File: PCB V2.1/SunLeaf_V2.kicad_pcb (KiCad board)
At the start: 4 copper layers, 77 x 40 mm, 111 parts, among them IC1 ESP_09, J1 20021121-00010C4LF, J10 B4B-PH-K-S(LF)(SN), J11 B4B-PH-K-S(LF)(SN), J12 B4B-PH-K-S(LF)(SN), J13 B4B-PH-K-S(LF)(SN), J14 B4B-PH-K-S(LF)(SN), J15 B4B-PH-K-S(LF)(SN), J16 B4B-PH-K-S(LF)(SN), J2 0475890001-MicroUSBPort, J3 B2B-PH-K-S(LF)(SN), J4 B3B-PH-K-S(LF)(SN), J5 B4B-PH-K-S(LF)(SN), J6 B4B-PH-K-S(LF)(SN), J7 B4B-PH-K-S(LF)(SN), J8 B4B-PH-K-S(LF)(SN), J9 B4B-PH-K-S(LF)(SN), P1 CONN_01X04, Q1 DMG2307L-7, Q2 DMG2307L-7, SW1 B3U-1000P, SW2 B3U-1000P, T1 1909763-1, U1 STM32F446RET6_-_TQFP64, U2 BQ24210DQCT, U3 AZ1117CR-3.3TRG1_1, U4 74HC4052D, U5 PCA9518DBQR, X1 ABM3B8.000MHZB2T, X2 ABS07-32.768KHZ-9-T

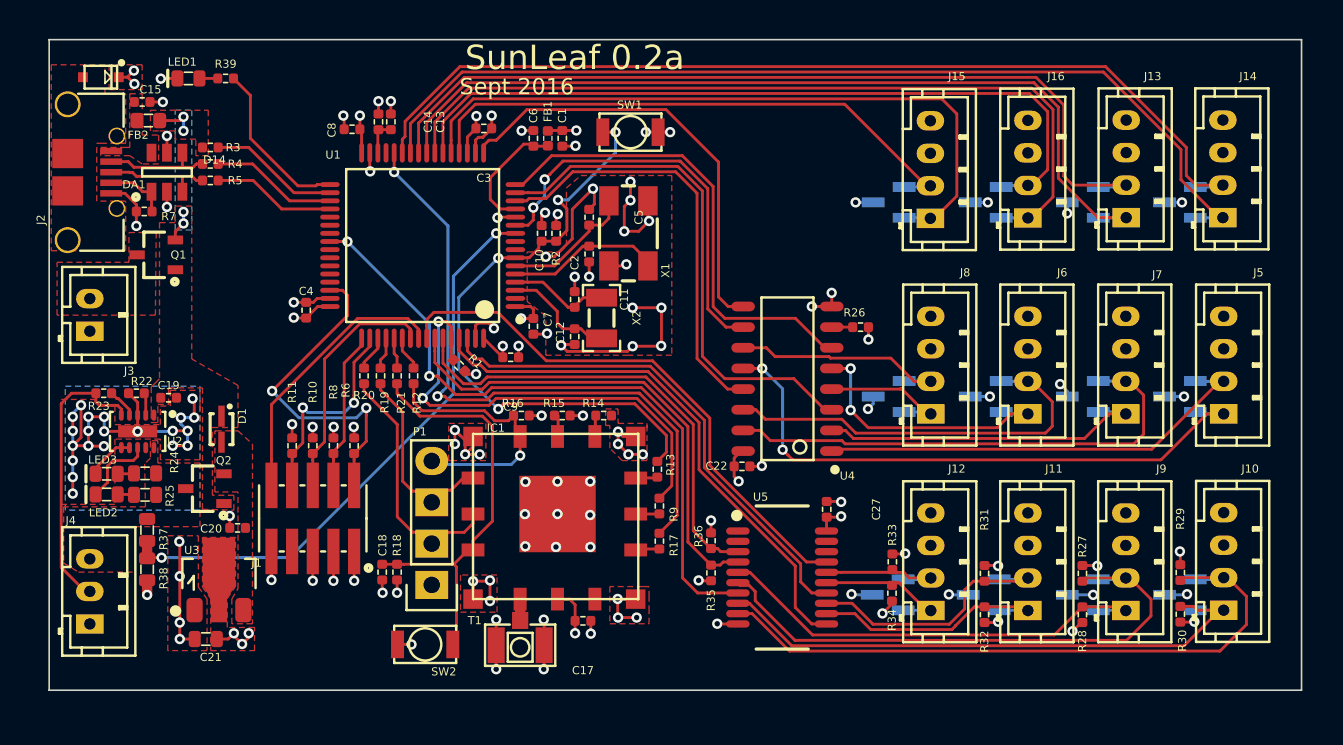
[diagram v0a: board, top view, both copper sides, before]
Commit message: App Notes
App notes added to datasheets folder.
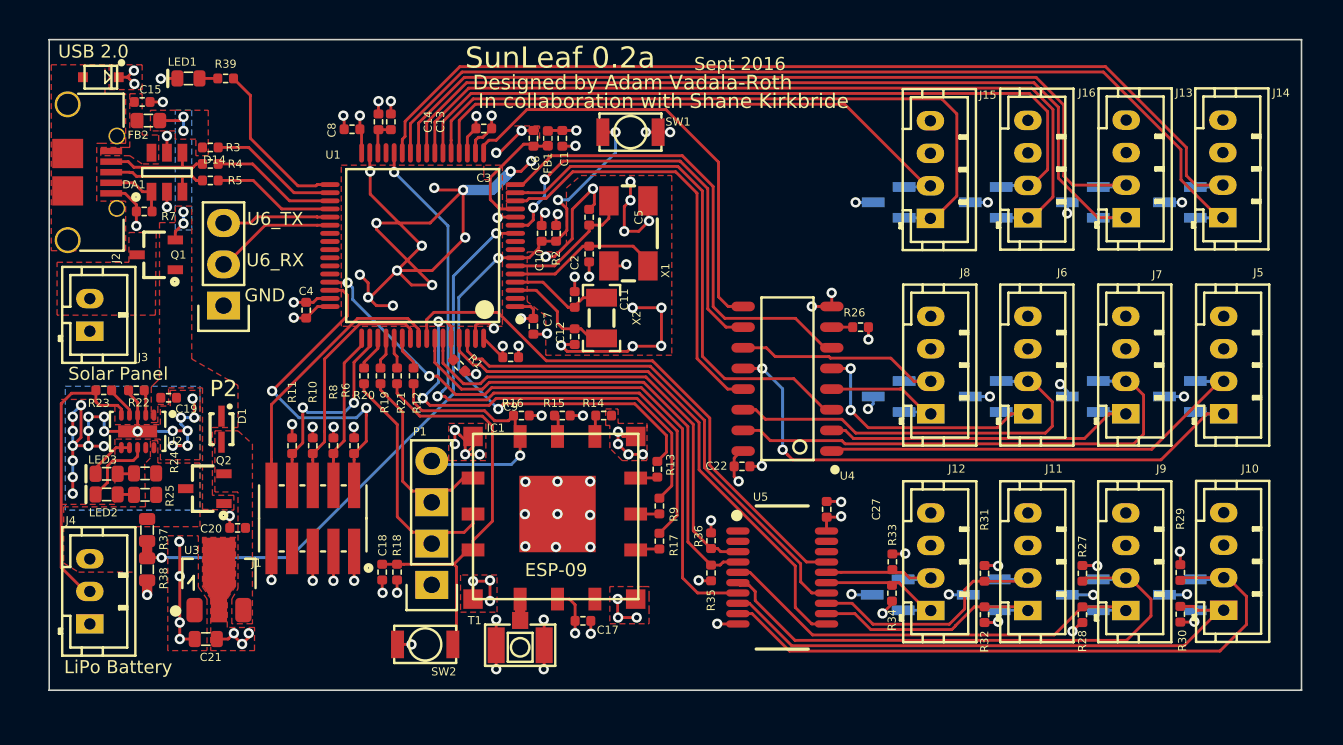
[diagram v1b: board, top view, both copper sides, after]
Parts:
- added P2: CONN_01X03, Pin_Headers:Pin_Header_Straight_1x03, F.Cu at (53.7, 46.4)
- moved R22 0.18 mm to (48.4, 51.6)
- moved R23 0.18 mm to (46.4, 51.6)
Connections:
- U1 pad 37: Net-(U1-Pad37) -> /MCU-STM32F446RET6/UART6_TX
- U1 pad 38: Net-(U1-Pad38) -> /MCU-STM32F446RET6/UART6_RX
- U1 pad 40: /I2C Grove Sensors/EN1_IMUX -> Net-(U1-Pad40)
- U1 pad 45: Net-(U1-Pad45) -> /I2C Grove Sensors/EN1_IMUX
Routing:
- net GND: track 152.9 -> 197.6 mm, vias 114 -> 127
- net /MCU-STM32F446RET6/UART6_RX: track 0.00 -> 7.61 mm
- net /MCU-STM32F446RET6/UART6_TX: track 0.00 -> 6.71 mm
- net /I2C Grove Sensors/EN1_IMUX: track 41.6 -> 39.1 mm
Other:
- board text added: "3V3"
- board text added: "BAT_PWR"
- board text added: "BAT_THERM"
- board text added: "Designed by Adam Vadala-Roth"
- board text added: "ESP-09"
- board text added: "ESP_PGM_MODE"
- board text added: "ESP_RX"
- board text added: "ESP_TX"
- board text added: "GND"
- board text added: "In collaboration with Shane Kirkbride"
- board text added: "LiPo Battery"
- board text added: "SOLAR_V+"
- board text added: "Solar Panel"
- board text added: "U6_RX"
- board text added: "U6_TX"
- board text added: "USB 2.0"

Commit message: DRC Clearing
More DRC errors cleared. Getting board ready for fab.
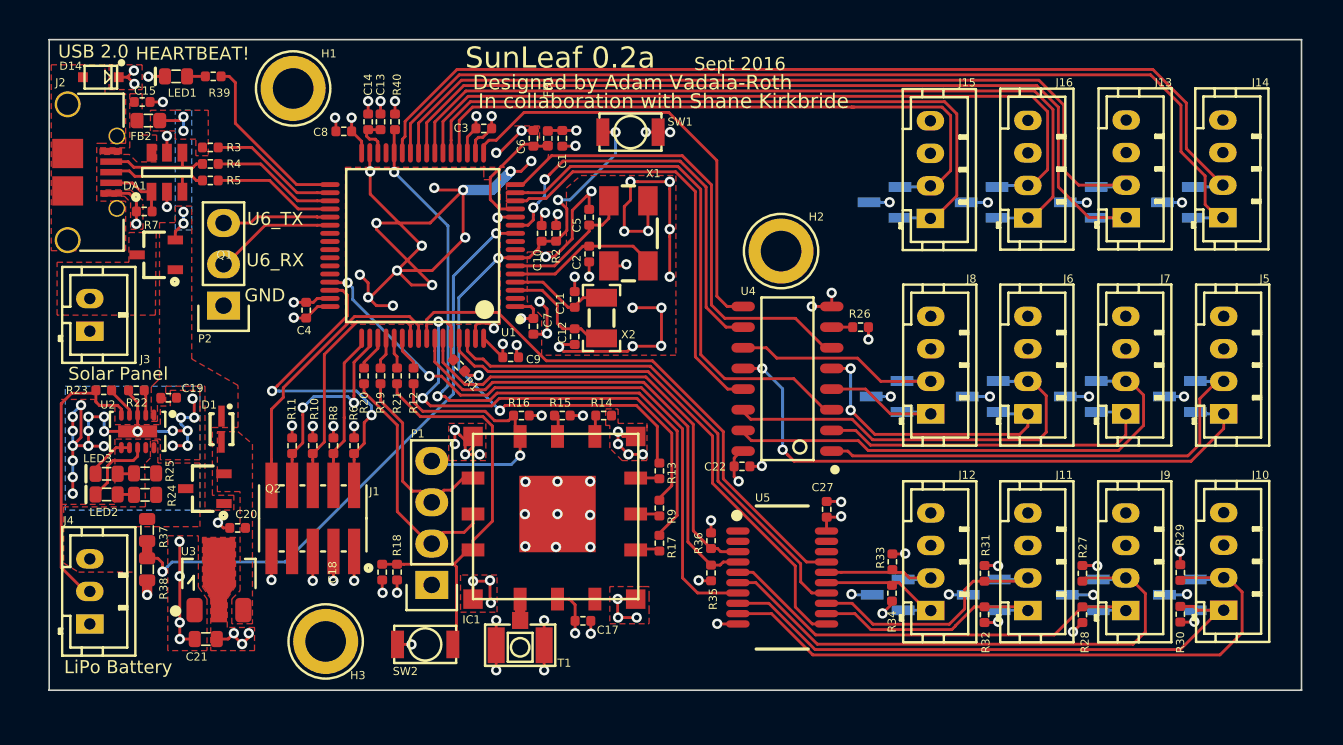
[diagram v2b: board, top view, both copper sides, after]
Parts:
- added H1: 1pin, Connect:1pin, F.Cu at (58.0, 33.0)
- added H2: 1pin, Connect:1pin, F.Cu at (88.0, 43.0)
- added H3: 1pin, Connect:1pin, F.Cu at (60.0, 67.0)
- added R40: RC1005F103CS, PCB_Footprints:R0402, F.Cu at (64.3, 35.1)
- moved LED1 0.77 mm to (50.8, 32.3)
- moved R39 0.77 mm to (53.1, 32.3)
- moved C14 0.64 mm to (62.6, 35.1)
- moved C13 0.63 mm to (63.4, 35.1)
- moved C8 0.52 mm to (61.1, 35.6)
- moved D10 0.25 mm to (100.3, 40.0)
- moved D11 0.25 mm to (94.4, 40.0)
- moved D4 0.19 mm to (100.4, 51.9)
- moved R13 0.16 mm to (80.5, 56.5)
- moved D12 0.13 mm to (112.4, 40.0)
- moved R17 0.13 mm to (80.5, 61.0)
- moved R9 0.13 mm to (80.5, 58.8)
- moved D13 0.13 mm to (106.4, 40.0)
- moved D2 0.13 mm to (94.5, 51.9)
- moved D3 0.13 mm to (106.4, 51.9)
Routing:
- net GND: track 197.6 -> 211.0 mm, vias 127 -> 130
- net /Analog and Digital Grove IO/ANIO_4: track 35.2 -> 39.8 mm
- net /UART Grove Sensors/UART_TX0: track 27.7 -> 29.6 mm
- net /MCU-STM32F446RET6/ESPTOST_BOOT1: track 39.3 -> 40.8 mm
- net /Analog and Digital Grove IO/ANIO_3: track 59.6 -> 61.0 mm
- net +3V3: track 40.0 -> 41.2 mm, vias 31 -> 32
- net /MCU-STM32F446RET6/BAT_VOLT: track 36.2 -> 37.2 mm
- net /UART Grove Sensors/UART_RX2: track 20.8 -> 21.8 mm
- net /UART Grove Sensors/UART_RX1: track 17.2 -> 18.0 mm
- net Net-(C13-Pad1): track 2.20 -> 2.96 mm
- net /MCU-STM32F446RET6/HEARTBEAT: track 10.2 -> 10.9 mm
- net /UART Grove Sensors/UART_RX0: track 37.2 -> 37.8 mm
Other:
- board text added: "HEARTBEAT!"
- board text removed: "ESP-09"

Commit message: DRC clear
all design rule violations cleared.
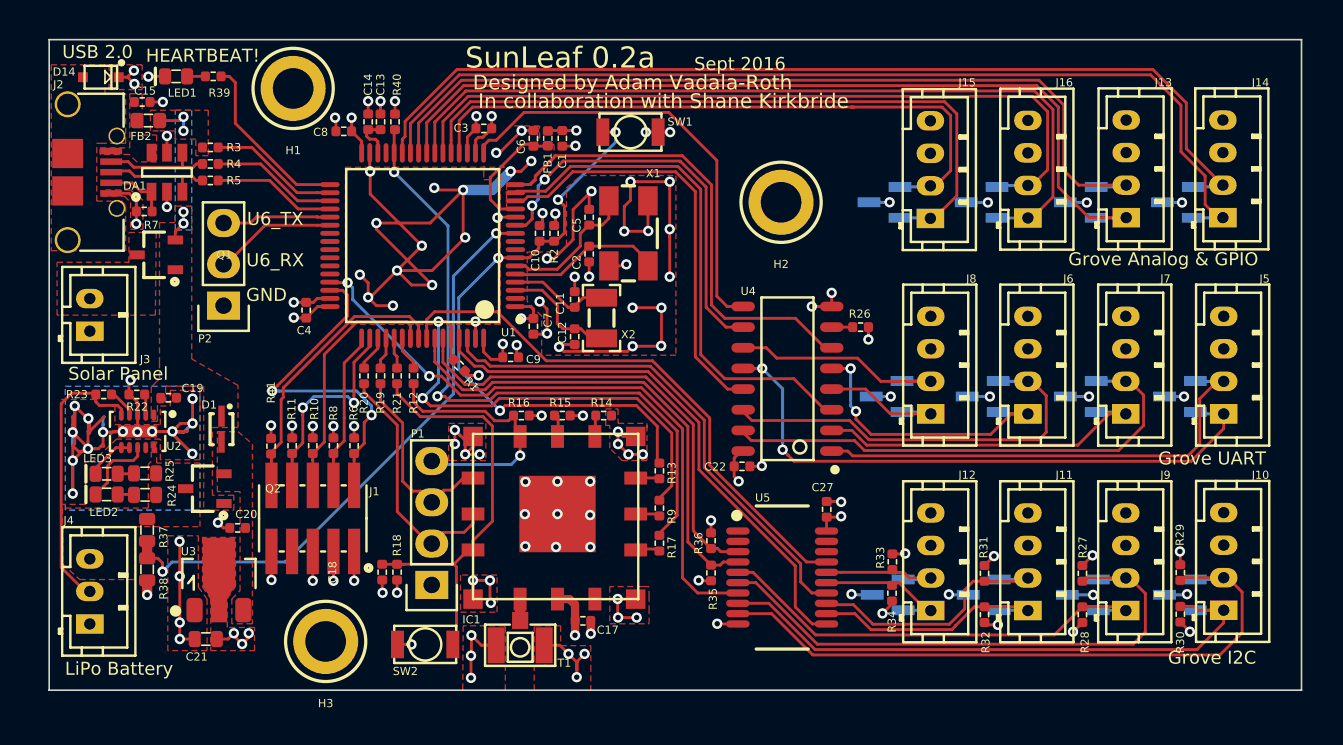
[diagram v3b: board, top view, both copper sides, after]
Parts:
- added R41: RC1005F102CS, PCB_Footprints:R0402, F.Cu at (56.6, 55.0)
- H1, H2, H3: value 1pin -> M2.5_Hole; footprint Connect:1pin -> PCB_Footprints:M2.5_HOLE
- moved H2 3.00 mm to (88.0, 40.0)
- moved R22 0.26 mm to (48.4, 51.8)
- moved R23 0.25 mm to (46.4, 51.8)
- moved R2 0.13 mm to (74.0, 41.9)
- moved C10 0.13 mm to (73.2, 41.9)
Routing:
- net GND: track 211.0 -> 233.7 mm, vias 130 -> 126
- net +3V3: track 41.2 -> 42.6 mm, vias 32 -> 33
- net /UART Grove Sensors/UART_RX2: track 21.8 -> 21.0 mm
- net /MCU-STM32F446RET6/ESP_ST_RST: track 38.0 -> 37.5 mm
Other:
- board text added: "Grove Analog & GPIO"
- board text added: "Grove I2C"
- board text added: "Grove UART"
- board text added: "SOL_V+"
- board text removed: "SOLAR_V+"

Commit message: 3D and Tweaks
3D files added for components for proper 3D rneder of the board. Board
tweaked, additional ground pours and sticking under neath the ESP-09,
cleaned up routign of JTAG , added labeling of all the pin signals.
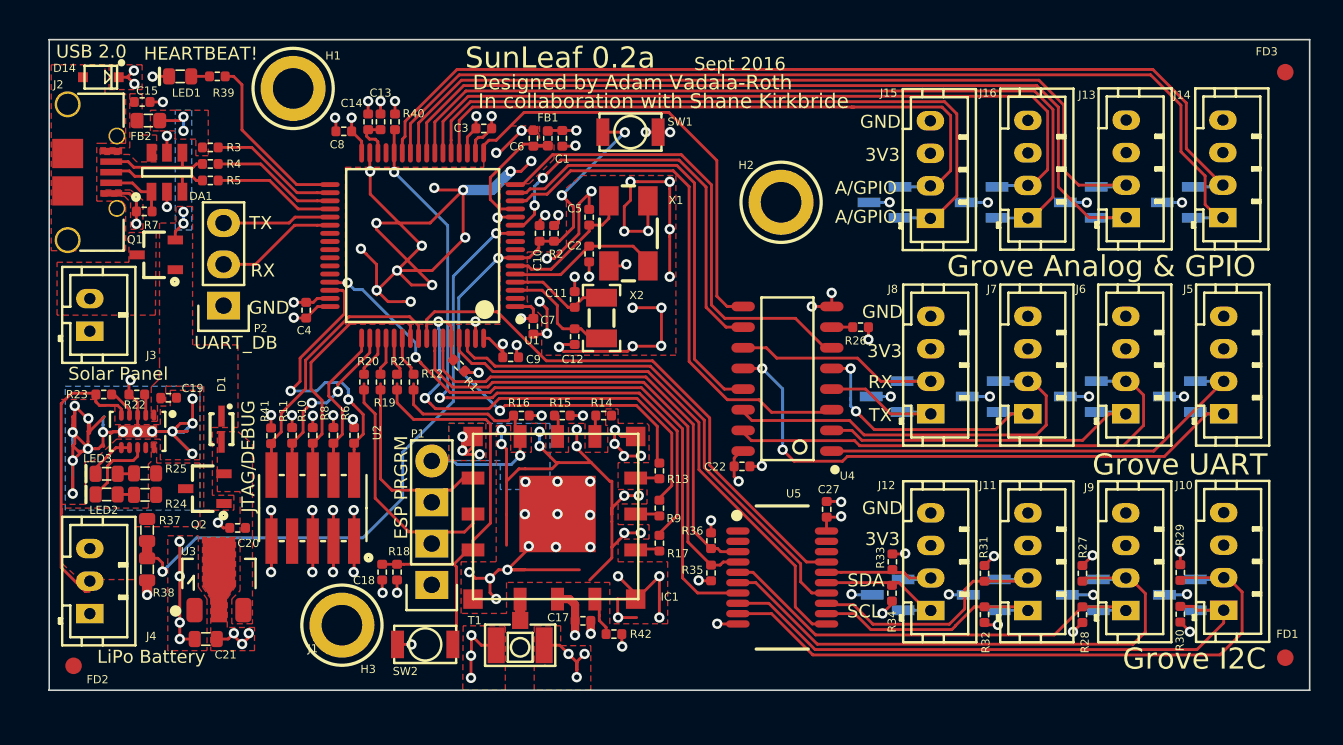
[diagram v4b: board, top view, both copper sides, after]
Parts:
- added FD1: FIDUCIAL, PCB_Footprints:FIDUCIAL, F.Cu at (119.0, 68.0)
- added FD2: FIDUCIAL, PCB_Footprints:FIDUCIAL, F.Cu at (44.5, 68.5)
- added FD3: FIDUCIAL, PCB_Footprints:FIDUCIAL, F.Cu at (119.0, 32.0)
- added R42: RC1005F103CS, PCB_Footprints:R0402, F.Cu at (77.7, 66.5)
- moved H3 1.41 mm to (61.0, 66.0)
- moved J4 0.64 mm to (45.5, 65.3)
- moved R10 0.64 mm to (59.2, 54.3)
- moved R11 0.64 mm to (57.9, 54.3)
- moved R6 0.64 mm to (61.7, 54.3)
- moved R8 0.64 mm to (60.5, 54.3)
- moved J1 0.63 mm to (59.2, 58.8)
- moved R41 0.63 mm to (56.6, 54.4)
- moved R12 0.38 mm to (65.4, 51.1)
- moved R19 0.38 mm to (63.4, 51.1)
- moved R20 0.38 mm to (62.4, 51.1)
- moved R21 0.38 mm to (64.4, 51.1)
- moved LED1 0.25 mm to (51.1, 32.3)
- moved R39 0.25 mm to (53.3, 32.3)
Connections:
- D2 pad 1: /UART Grove Sensors/UART_TX3 -> /UART Grove Sensors/UART_RX3
- D2 pad 2: /UART Grove Sensors/UART_RX3 -> /UART Grove Sensors/UART_TX3
- D3 pad 1: /UART Grove Sensors/UART_TX2 -> /UART Grove Sensors/UART_RX2
- D3 pad 2: /UART Grove Sensors/UART_RX2 -> /UART Grove Sensors/UART_TX2
- D4 pad 1: /UART Grove Sensors/UART_TX1 -> /UART Grove Sensors/UART_RX1
- D4 pad 2: /UART Grove Sensors/UART_RX1 -> /UART Grove Sensors/UART_TX1
- D5 pad 1: /UART Grove Sensors/UART_TX0 -> /UART Grove Sensors/UART_RX0
- D5 pad 2: /UART Grove Sensors/UART_RX0 -> /UART Grove Sensors/UART_TX0
- J5 pad 1: /UART Grove Sensors/UART_RX0 -> /UART Grove Sensors/UART_TX0
- J5 pad 2: /UART Grove Sensors/UART_TX0 -> /UART Grove Sensors/UART_RX0
- J6 pad 1: /UART Grove Sensors/UART_RX1 -> /UART Grove Sensors/UART_TX1
- J6 pad 2: /UART Grove Sensors/UART_TX1 -> /UART Grove Sensors/UART_RX1
- J7 pad 1: /UART Grove Sensors/UART_RX2 -> /UART Grove Sensors/UART_TX2
- J7 pad 2: /UART Grove Sensors/UART_TX2 -> /UART Grove Sensors/UART_RX2
- J8 pad 1: /UART Grove Sensors/UART_RX3 -> /UART Grove Sensors/UART_TX3
- J8 pad 2: /UART Grove Sensors/UART_TX3 -> /UART Grove Sensors/UART_RX3
- U4 pad 1: /UART Grove Sensors/UART_TX0 -> /UART Grove Sensors/UART_RX0
- U4 pad 11: /UART Grove Sensors/UART_TX3 -> /UART Grove Sensors/UART_RX3
- U4 pad 12: /UART Grove Sensors/UART_RX0 -> /UART Grove Sensors/UART_TX0
- U4 pad 13: /UART Grove Sensors/UART_S_RX -> /MCU-STM32F446RET6/UART_S_RX
- U4 pad 14: /UART Grove Sensors/UART_TX1 -> /UART Grove Sensors/UART_RX1
- U4 pad 15: /UART Grove Sensors/UART_TX2 -> /UART Grove Sensors/UART_RX2
- U4 pad 2: /UART Grove Sensors/UART_RX2 -> /UART Grove Sensors/UART_TX2
- U4 pad 3: /MCU-STM32F446RET6/UART_S_RX -> /UART Grove Sensors/UART_S_RX
- U4 pad 4: /UART Grove Sensors/UART_RX3 -> /UART Grove Sensors/UART_TX3
- U4 pad 5: /UART Grove Sensors/UART_RX1 -> /UART Grove Sensors/UART_TX1
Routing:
- net (no net): track 0.00 -> 30.7 mm, vias 0 -> 10
- net GND: track 233.7 -> 256.5 mm, vias 126 -> 130
- net /UART Grove Sensors/UART_TX2: track 30.9 -> 20.7 mm
- net /UART Grove Sensors/UART_RX0: track 37.8 -> 27.7 mm, vias 2 -> 0
- net /UART Grove Sensors/UART_RX2: track 21.0 -> 30.7 mm
- net /UART Grove Sensors/UART_TX1: track 25.1 -> 17.2 mm, vias 0 -> 2
- net /UART Grove Sensors/UART_TX0: track 29.6 -> 37.2 mm, vias 0 -> 2
- net /UART Grove Sensors/UART_S_RX: track 26.2 -> 33.7 mm
- net /UART Grove Sensors/UART_RX1: track 17.7 -> 24.6 mm, vias 2 -> 0
- net /UART Grove Sensors/UART_TX3: track 14.2 -> 8.53 mm
- net /UART Grove Sensors/UART_RX3: track 8.53 -> 14.2 mm
- net /MCU-STM32F446RET6/UART_S_RX: track 32.3 -> 26.7 mm
- net /MCU-STM32F446RET6/SWDIO_TMS: track 20.9 -> 18.2 mm
- net Net-(IC1-Pad16): track 0.00 -> 2.43 mm
- net +3V3: track 42.6 -> 44.8 mm, vias 33 -> 35
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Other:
- board size 77 x 40 mm -> 77.5 x 40 mm
- board text added: "A/GPIO"
- board text added: "ESP PRGRM"
- board text added: "IO0/A0"
- board text added: "IO1/A1"
- board text added: "IO2/A2"
- board text added: "IO3/A3"
- board text added: "IO4/A4"
- board text added: "IO5/A5"
- board text added: "IO6/IO6"
- board text added: "IO7/A7"
- board text added: "JTAG/DEBUG"
- board text added: "RX"
- board text added: "RX0"
- board text added: "RX1"
- board text added: "RX2"
- board text added: "RX3"
- board text added: "SCL"
- board text added: "SCL0"
- board text added: "SCL1"
- board text added: "SCL2"
- board text added: "SCL3"
- board text added: "SDA"
- board text added: "SDA0"
- board text added: "SDA1"
- board text added: "SDA2"
- board text added: "SDA3"
- board text added: "TX"
- board text added: "TX0"
- board text added: "TX1"
- board text added: "TX2"
- board text added: "TX3"
- board text added: "UART_DB"
